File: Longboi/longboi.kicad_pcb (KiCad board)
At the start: 2 copper layers, 383 x 78.2 mm, 190 parts, among them J2 ICSP_Header, K0 KEYSW, K1 KEYSW, K10 KEYSW, K11 KEYSW, K12 KEYSW, K13 KEYSW, K14 KEYSW, K15 KEYSW, K16 KEYSW, K17 KEYSW, K18 KEYSW, K19 KEYSW, K2 KEYSW, K20 KEYSW, K21 KEYSW, K22 KEYSW, K22-spacer1 KEYSW, K22-stepped1 KEYSW, K23 KEYSW, K24 KEYSW, K25 KEYSW, K26 KEYSW, K27 KEYSW, K28 KEYSW, K29 KEYSW, K3 KEYSW, K3-2uVert1 KEYSW, K30 KEYSW, K31 KEYSW, K32 KEYSW, K33 KEYSW, K34 KEYSW, K35 KEYSW, K36 KEYSW, K37 KEYSW, K38 KEYSW, K38-2uVert1 KEYSW, K39 KEYSW, K39-spacer1 KEYSW, K4 KEYSW, K4-spacer1 KEYSW, K40 KEYSW, K41 KEYSW, K42 KEYSW, K43 KEYSW, K44 KEYSW, K45 KEYSW, K46 KEYSW, K47 KEYSW, K48 KEYSW, K49 KEYSW, K5 KEYSW, K50 KEYSW, K51 KEYSW, K52 KEYSW, K52-1u1 KEYSW, K52-2u1 KEYSW, K53 KEYSW, K54 KEYSW, K55 KEYSW, K55-1.25 KEYSW, K55-spacer1 KEYSW, K56 KEYSW, K56-1.25 KEYSW, K57 KEYSW, K57-1.25 KEYSW, K57-1.5u1 KEYSW, K57-1u1 KEYSW, K58 KEYSW, K58-6u1 KEYSW, K58for1.25Row1 KEYSW, K59 KEYSW, K59-1.25u1 KEYSW, K59-7u1 KEYSW, K59Alt1 KEYSW, K6 KEYSW, K60 KEYSW, K60Alt1 KEYSW, K61 KEYSW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

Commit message: update longboi to be slightly newer than ordered
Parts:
- added H6: MountingHole, random-keyboard-parts:M2 Mounting Hole, F.Cu at (395.9, 95.6)
- added H7: MountingHole, random-keyboard-parts:M2 Mounting Hole, F.Cu at (16.7, 21.2)
- added H8: MountingHole, random-keyboard-parts:M2 Mounting Hole, F.Cu at (16.7, 95.6)
- added H9: MountingHole, random-keyboard-parts:M2 Mounting Hole, F.Cu at (395.9, 21.2)
- added K61-1.25u1: KEYSW, MX_Only:MXOnly-1.25U-NoLED, F.Cu at (294.4, 87.0)
- added K62-1.25u1: KEYSW, MX_Only:MXOnly-1.25U-NoLED, F.Cu at (318.2, 87.0)
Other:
- board text added: ".5u blocker"

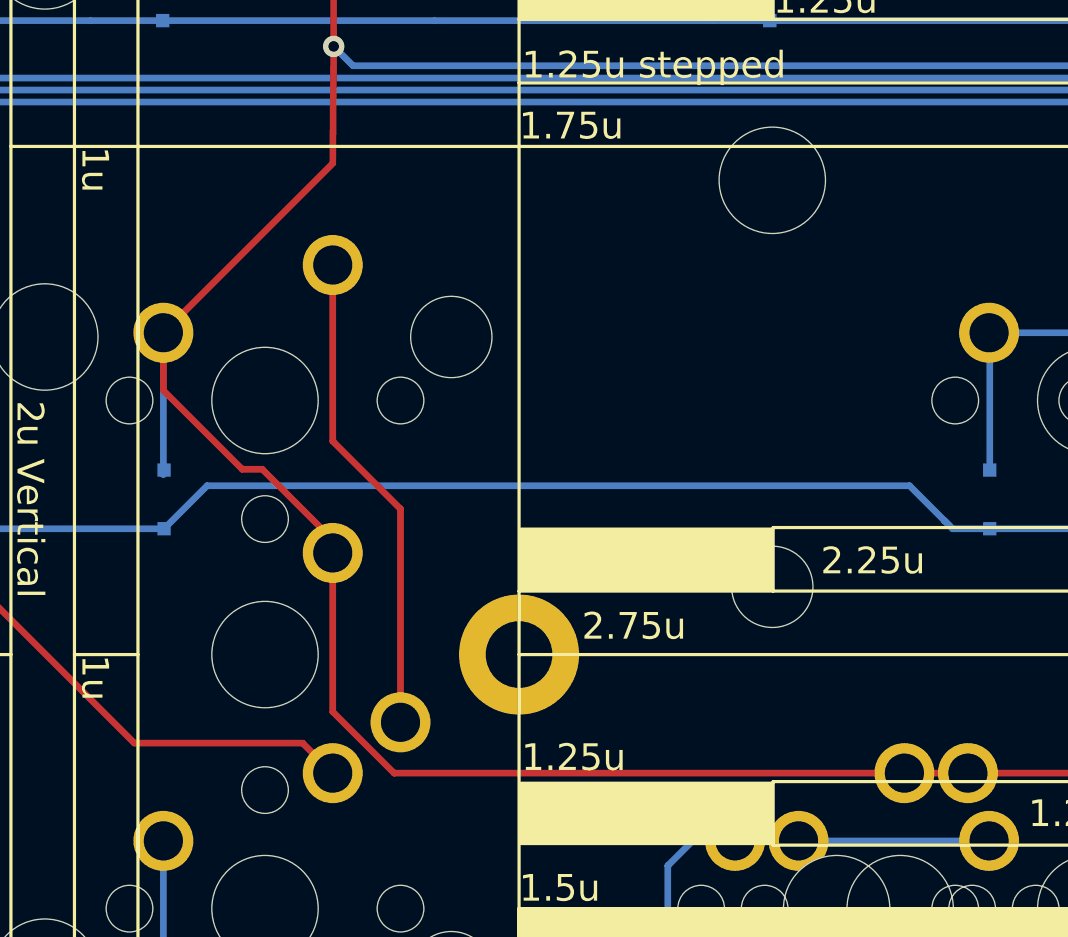
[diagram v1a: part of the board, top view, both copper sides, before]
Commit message: fix bug in longboi...
key38 was not schematiced right
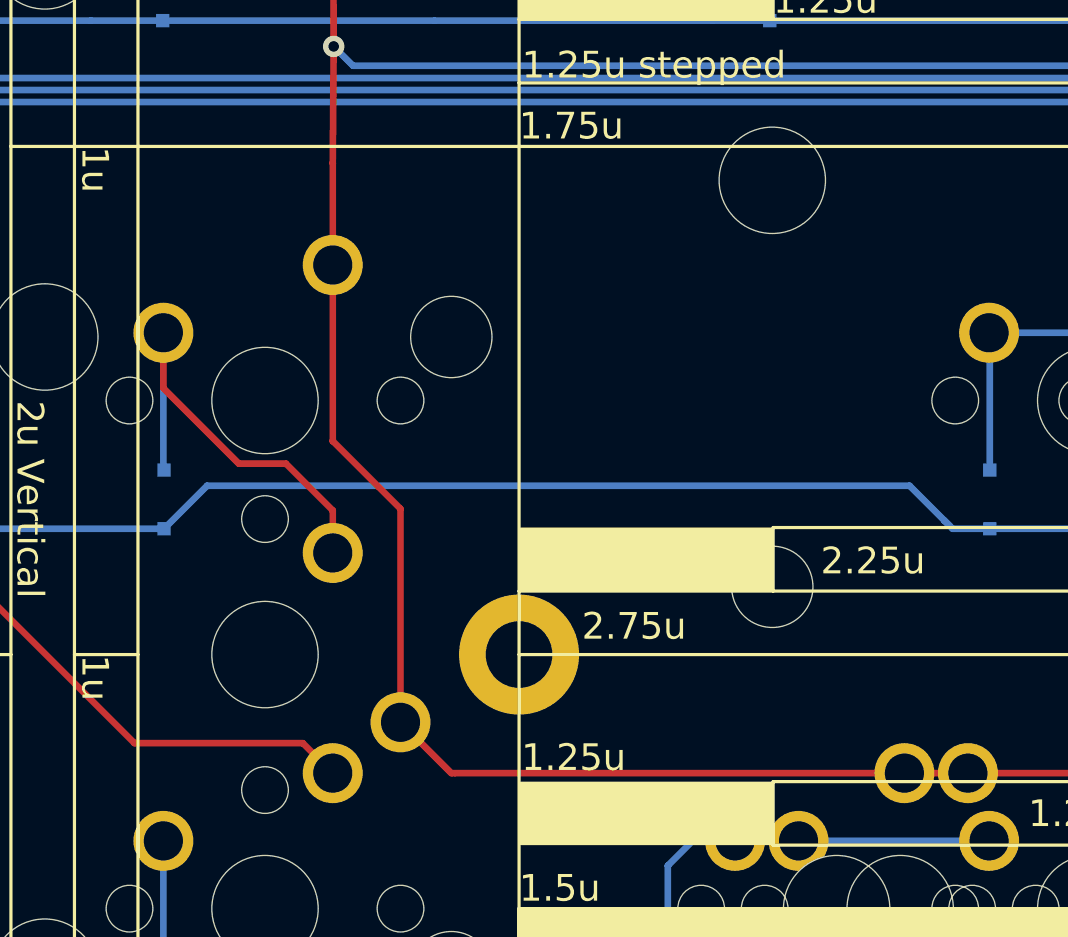
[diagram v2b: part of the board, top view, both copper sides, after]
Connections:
- D38 pad 2: /Col_3 -> Net-(D38-Pad2)
- K38 pad 1: /Col_3 -> Net-(D38-Pad2)
- K38 pad 2: Net-(K38-2uVert1-Pad2) -> /Col_3
- K38-2uVert1 pad 1: /Col_3 -> Net-(D38-Pad2)
- K38-2uVert1 pad 2: Net-(K38-2uVert1-Pad2) -> /Col_3
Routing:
- net Net-(K38-2uVert1-Pad2): track 18.2 -> 0.00 mm
- net Net-(D38-Pad2): track 0.00 -> 17.1 mm
- net /Col_3: track 347.6 -> 335.4 mm
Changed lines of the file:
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@@
   (net 110 "Rotary_A")
   (net 111 "Rotary_B")
-  (net 112 "Net-(K38-2uVert1-Pad2)")
+  (net 112 "Net-(D38-Pad2)")
   (footprint "MX_Only:MXOnly-1U-NoLED" (layer "F.Cu")
     (at 368.18375 67.945)
@@
     (pad "" np_thru_hole circle locked (at -5.08 0 48.0996) (size 1.75 1.75) (drill 1.75) (layers *.Cu *.Mask))
     (pad "1" thru_hole circle locked (at -3.81 -2.54) (size 2.25 2.25) (drill 1.47) (layers *.Cu *.Mask)
-      (net 17 "/Col_3") (pinfunction "1") (pintype "passive"))
+      (net 112 "Net-(D38-Pad2)") (pinfunction "1") (pintype "passive"))
     (pad "2" thru_hole circle locked (at 2.54 -5.08) (size 2.25 2.25) (drill 1.47) (layers *.Cu *.Mask)
-      (net 112 "Net-(K38-2uVert1-Pad2)") (pinfunction "2") (pintype "passive"))
+      (net 17 "/Col_3") (pinfunction "2") (pintype "passive"))
   )
   (footprint "MX_Only:MXOnly-1U-NoLED" (layer "F.Cu")
@@
     (pad "" np_thru_hole circle locked (at 0 0 270) (size 3.9878 3.9878) (drill 3.9878) (layers *.Cu *.Mask))
     (pad "1" thru_hole circle locked (at -3.81 -2.54 270) (size 2.25 2.25) (drill 1.47) (layers *.Cu *.Mask)
-      (net 17 "/Col_3") (pinfunction "1") (pintype "passive"))
+      (net 112 "Net-(D38-Pad2)") (pinfunction "1") (pintype "passive"))
     (pad "2" thru_hole circle locked (at 2.54 -5.08 270) (size 2.25 2.25) (drill 1.47) (layers *.Cu *.Mask)
-      (net 112 "Net-(K38-2uVert1-Pad2)") (pinfunction "2") (pintype "passive"))
+      (net 17 "/Col_3") (pinfunction "2") (pintype "passive"))
   )
   (footprint "MX_Only:MXOnly-1.25U-NoLED" (layer "F.Cu")
@@
       (net 11 "/Row_2") (pinfunction "K") (pintype "passive"))
     (pad "2" smd rect locked (at 1.1 0 90) (size 0.5 0.5) (layers "B.Cu" "B.Paste" "B.Mask")
-      (net 17 "/Col_3") (pinfunction "A") (pintype "passive"))
+      (net 112 "Net-(D38-Pad2)") (pinfunction "A") (pintype "passive"))
     (model "${KICAD6_3DMODEL_DIR}/Diode_SMD.3dshapes/D_SOD-323F.wrl"
       (offset (xyz 0 0 0))
@@
   (segment (start 206.38404 58.8769) (end 208.952151 61.445011) (width 0.25) (layer "B.Cu") (net 16))
   (segment (start 213.238519 61.445011) (end 215.80663 58.8769) (width 0.25) (layer "B.Cu") (net 16))
-  (segment (start 84.97375 73.66) (end 84.97375 73.162909) (width 0.25) (layer "F.Cu") (net 17))
-  (segment (start 87.272748 81.915) (end 106.405 81.915) (width 0.25) (layer "F.Cu") (net 17))
+  (segment (start 87.51375 72.009) (end 87.51375 80.01) (width 0.25) (layer "F.Cu") (net 17))
+  (segment (start 87.51375 80.01) (end 89.41875 81.915) (width 0.25) (layer "F.Cu") (net 17))
   (segment (start 85.04995 43.7388) (end 85.04995 39.3192) (width 0.25) (layer "F.Cu") (net 17))
   (segment (start 84.97375 43.815) (end 85.04995 43.7388) (width 0.25) (layer "F.Cu") (net 17))
@@
   (segment (start 115.93 81.915) (end 108.78625 81.915) (width 0.25) (layer "F.Cu") (net 17))
   (segment (start 108.78625 81.915) (end 106.405 81.915) (width 0.25) (layer "F.Cu") (net 17))
-  (segment (start 84.97375 79.616002) (end 87.272748 81.915) (width 0.25) (layer "F.Cu") (net 17))
+  (segment (start 84.97375 69.469) (end 87.51375 72.009) (width 0.25) (layer "F.Cu") (net 17))
   (segment (start 87.51375 41.91) (end 85.60875 43.815) (width 0.25) (layer "F.Cu") (net 17))
   (segment (start 87.25 37.11915) (end 87.25 34.1) (width 0.25) (layer "F.Cu") (net 17))
+  (segment (start 89.41875 81.915) (end 89.56375 81.915) (width 0.25) (layer "F.Cu") (net 17))
   (segment (start 87.25 34.1) (end 84.97375 31.82375) (width 0.25) (layer "F.Cu") (net 17))
-  (segment (start 84.97375 73.66) (end 84.97375 79.616002) (width 0.25) (layer "F.Cu") (net 17))
+  (segment (start 89.56375 81.915) (end 106.405 81.915) (width 0.25) (layer "F.Cu") (net 17))
   (segment (start 84.97375 43.815) (end 85.00875 54.67) (width 0.25) (layer "F.Cu") (net 17))
-  (segment (start 84.97375 59.055) (end 78.62375 65.405) (width 0.25) (layer "F.Cu") (net 17))
   (segment (start 85.04995 39.3192) (end 87.25 37.11915) (width 0.25) (layer "F.Cu") (net 17))
+  (segment (start 84.97375 62.865) (end 84.97375 69.469) (width 0.25) (layer "F.Cu") (net 17))
   (segment (start 85.60875 43.815) (end 84.97375 43.815) (width 0.25) (layer "F.Cu") (net 17))
-  (segment (start 82.332453 70.521612) (end 81.578388 70.521612) (width 0.25) (layer "F.Cu") (net 17))
-  (segment (start 84.97375 73.162909) (end 82.332453 70.521612) (width 0.25) (layer "F.Cu") (net 17))
   (segment (start 84.97375 31.82375) (end 84.97375 24.765) (width 0.25) (layer "F.Cu") (net 17))
-  (segment (start 81.578388 70.521612) (end 78.62375 67.566974) (width 0.25) (layer "F.Cu") (net 17))
-  (segment (start 78.62375 67.566974) (end 78.62375 65.405) (width 0.25) (layer "F.Cu") (net 17))
+  (segment (start 84.97375 59.055) (end 84.97375 62.865) (width 0.25) (layer "F.Cu") (net 17))
   (via (at 85.00875 54.67) (size 0.8) (drill 0.4) (layers "F.Cu" "B.Cu") (net 17))
-  (segment (start 78.62375 70.73) (end 78.62375 65.405) (width 0.25) (layer "B.Cu") (net 17))
   (segment (start 128.958793 55.394511) (end 85.733261 55.394511) (width 0.25) (layer "B.Cu") (net 17))
   (segment (start 85.733261 55.394511) (end 85.00875 54.67) (width 0.25) (layer "B.Cu") (net 17))
@@
   (segment (start 334.07155 55.5879) (end 333.37615 55.8769) (width 0.25) (layer "B.Cu") (net 111))
   (segment (start 333.37615 55.8769) (end 332.61655 55.8769) (width 0.25) (layer "B.Cu") (net 111))
-  (segment (start 87.51375 72.009) (end 87.51375 80.01) (width 0.25) (layer "F.Cu") (net 112))
-  (segment (start 84.97375 69.469) (end 87.51375 72.009) (width 0.25) (layer "F.Cu") (net 112))
-  (segment (start 84.97375 62.865) (end 84.97375 69.469) (width 0.25) (layer "F.Cu") (net 112))
+  (segment (start 84.97375 73.66) (end 84.97375 72.06901) (width 0.25) (layer "F.Cu") (net 112))
+  (segment (start 84.97375 72.06901) (end 83.218161 70.313421) (width 0.25) (layer "F.Cu") (net 112))
+  (segment (start 81.452717 70.313421) (end 78.62375 67.484454) (width 0.25) (layer "F.Cu") (net 112))
+  (segment (start 83.218161 70.313421) (end 81.452717 70.313421) (width 0.25) (layer "F.Cu") (net 112))
+  (segment (start 78.62375 67.484454) (end 78.62375 65.405) (width 0.25) (layer "F.Cu") (net 112))
+  (segment (start 78.62375 65.405) (end 78.62375 70.528) (width 0.25) (layer "B.Cu") (net 112))
+  (segment (start 78.62375 70.528) (end 78.64915 70.5534) (width 0.25) (layer "B.Cu") (net 112))
   (zone (net 87) (net_name "Net-(D56-Pad2)") (layer "F.Cu") (hatch edge 0.508)
     (connect_pads (clearance 0.508))

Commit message: clean up map and string with prototype fixes
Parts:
- added D70: SOD-323F, Diode_SMD:D_SOD-323F, B.Cu at (40.5, 90.7)
- added Ge: LOGO, Images:beebo_10mm, F.Cu at (37.1, 56.9)
- added K55-spacer2: KEYSW, MX_Only:MXOnly-1U-NoLED, F.Cu at (111.0, 87.0)
- added K70: KEYSW, MX_Only:MXOnly-1U-NoLED, F.Cu at (44.3, 87.0)
- moved G1 0.31 mm to (202.5, 87.3)
- moved H8 0.14 mm to (16.8, 95.5)
- moved H7 0.14 mm to (16.8, 21.3)
- moved H6 0.14 mm to (395.8, 95.5)
- moved H9 0.14 mm to (395.8, 21.3)
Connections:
- K52-2u1 pad 2: /Col_1 -> /Col_2
- K53 pad 2: /Col_1 -> /Col_2
- K54 pad 2: /Col_2 -> /Col_3
- K55 pad 2: /Col_3 -> /Col_4
- K55-1.25 pad 2: /Col_3 -> /Col_4
- K55-spacer1 pad 2: /Col_3 -> /Col_4
- K56 pad 2: /Col_4 -> /Col_5
- K56-1.25 pad 2: /Col_4 -> /Col_5
- K57 pad 2: /Col_5 -> /Col_6
- K57-1.25 pad 2: /Col_5 -> /Col_6
- K57-1.5u1 pad 2: /Col_4 -> /Col_5
- K57-1u1 pad 2: /Col_5 -> /Col_6
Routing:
- net /Col_6: track 210.9 -> 238.6 mm
- net /Col_3: track 335.4 -> 309.5 mm
- net /Col_1: track 353.6 -> 342.1 mm
- net Net-(D70-Pad2): track 0.00 -> 6.07 mm
- net /Col_5: track 258.8 -> 263.2 mm
- net Net-(D61-Pad2): track 10.1 -> 13.2 mm
- net Net-(D62-Pad2): track 21.5 -> 19.4 mm
- net /Row_1: track 424.0 -> 426.0 mm
- net /Col_4: track 307.3 -> 308.0 mm
- net Net-(D56-Pad2): track 15.9 -> 15.3 mm

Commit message: moreupdates to tweak the two keyboards
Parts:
- removed K52-2u1: KEYSW, MX_Only:MXOnly-2U-ReversedStabilizers-NoLED
- added K0-2uVert1: KEYSW, MX_Only:MXOnly-2U-ReversedStabilizers-NoLED, F.Cu at (25.3, 39.4)
- added K35-2uVert1: KEYSW, MX_Only:MXOnly-2U-ReversedStabilizers-NoLED, F.Cu at (25.3, 77.5)
- added K54-2u1: KEYSW, MX_Only:MXOnly-2U-ReversedStabilizers-NoLED, F.Cu at (72.9, 87.0)
- added K70-2u1: KEYSW, MX_Only:MXOnly-2U-ReversedStabilizers-NoLED, F.Cu at (56.2, 87.0)
- moved Ge 62.0 mm to (98.3, 66.5)
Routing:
- net Net-(D0-Pad2): track 5.33 -> 17.2 mm
- net Net-(D70-Pad2): track 6.07 -> 18.0 mm
- net /Col_1: track 342.1 -> 354.0 mm
- net Net-(D35-Pad2): track 5.33 -> 16.6 mm
- net /Col_3: track 309.5 -> 319.5 mm
- net Net-(D53-Pad2): track 15.6 -> 6.07 mm
- net /Col_2: track 332.5 -> 323.0 mm
- net Net-(D54-Pad2): track 5.33 -> 14.8 mm
- net /Col_0: track 368.4 -> 373.6 mm
- net /Row_0: track 399.9 -> 401.2 mm
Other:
- board text added: "MountingHole"

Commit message: some more tweaks on keyboards
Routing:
- net /Col_2: track 323.0 -> 321.0 mm
- net /Row_2: track 448.2 -> 450.1 mm
- net Net-(D54-Pad2): track 14.8 -> 15.8 mm
- net Net-(D53-Pad2): track 6.07 -> 5.16 mm

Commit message: probably buying all three now
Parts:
- moved H6 1.41 mm to (394.8, 94.5)
- moved H7 1.41 mm to (17.8, 22.3)
- moved H8 1.41 mm to (17.8, 94.5)
- moved H9 1.41 mm to (394.8, 22.3)
- moved R3 1.01 mm to (350.6, 33.3)
- moved R5 1.01 mm to (338.5, 24.0)
- moved P1 1.01 mm to (349.2, 23.3)
- moved R6 1.01 mm to (356.7, 23.7)
- moved R2 1.01 mm to (348.6, 33.3)
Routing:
- net GND: track 207.4 -> 206.1 mm
- net Net-(R2-Pad1): track 32.0 -> 31.0 mm
- net Net-(R3-Pad1): track 32.8 -> 32.0 mm
- net Net-(F1-Pad2): track 14.5 -> 13.9 mm
- net Net-(P1-PadA5): track 11.1 -> 11.6 mm
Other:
- board size 383 x 78.2 mm -> 381 x 76.2 mm
